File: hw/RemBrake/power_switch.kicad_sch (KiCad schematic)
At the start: 54 parts, among them Q1 SiS415DNT, Q2 BC337, Q3 BC847, Q4 BC337, Q5 BC847, Q6 BC337, Q7 BC847, U1 TPS62140, U2 BD5230G-TR, U3 XC6220B331MR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

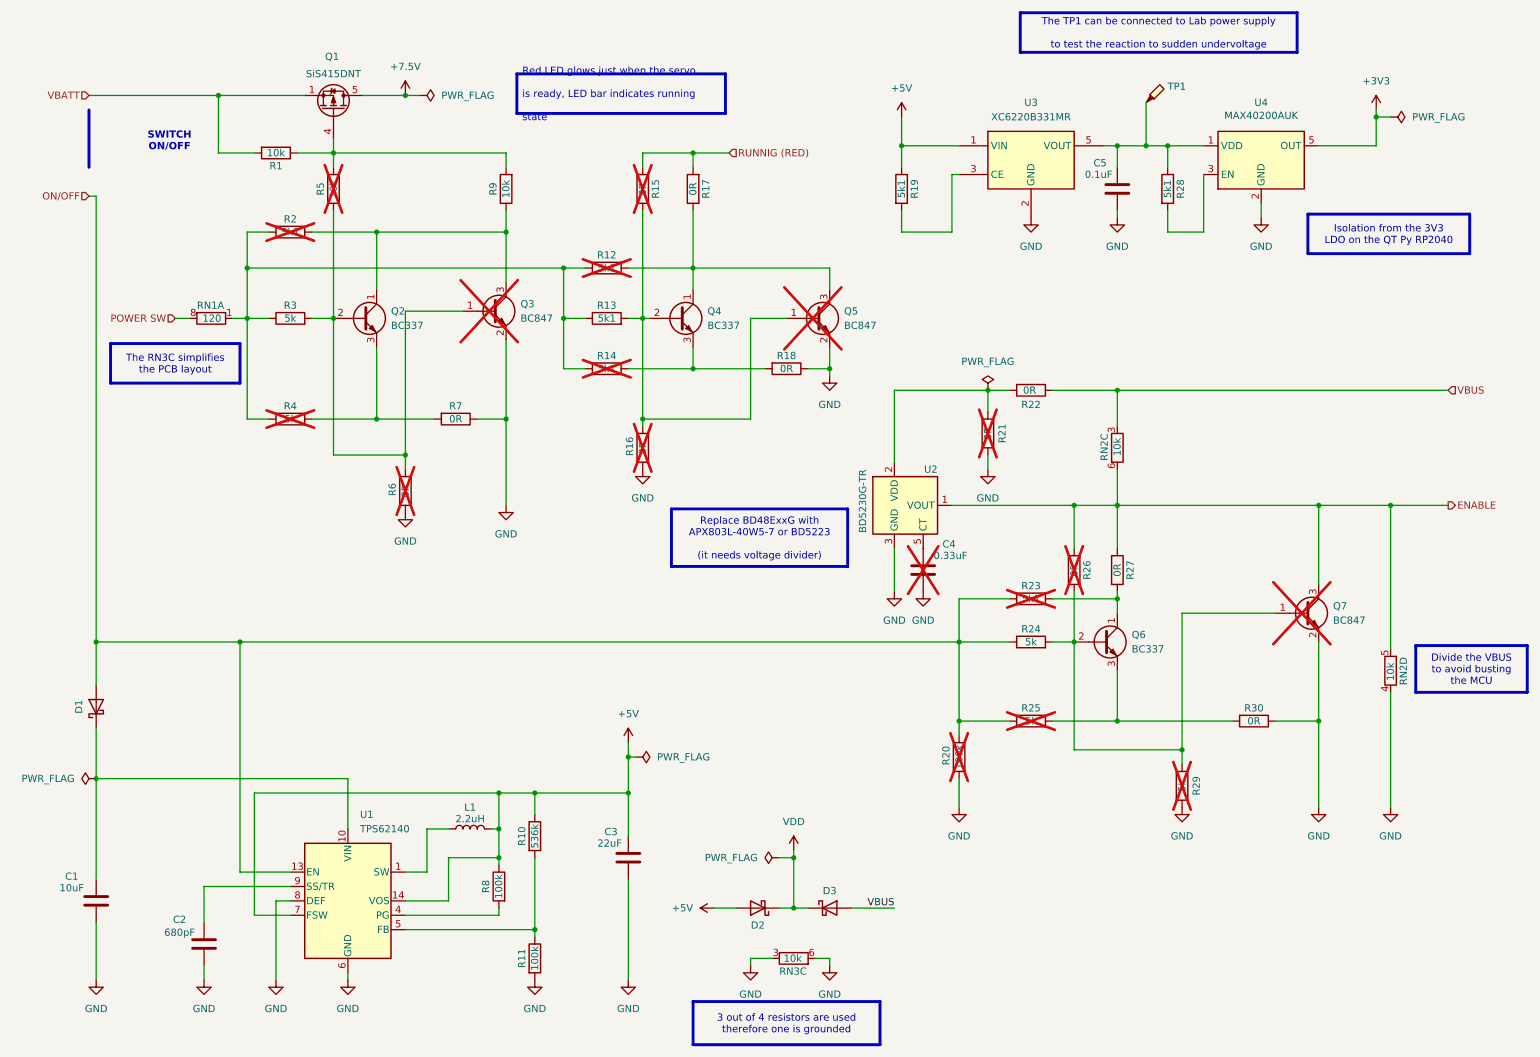
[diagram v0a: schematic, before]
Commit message: updated schematics and pcb - smd transistor was not connected to resistor to limit current through buzzer
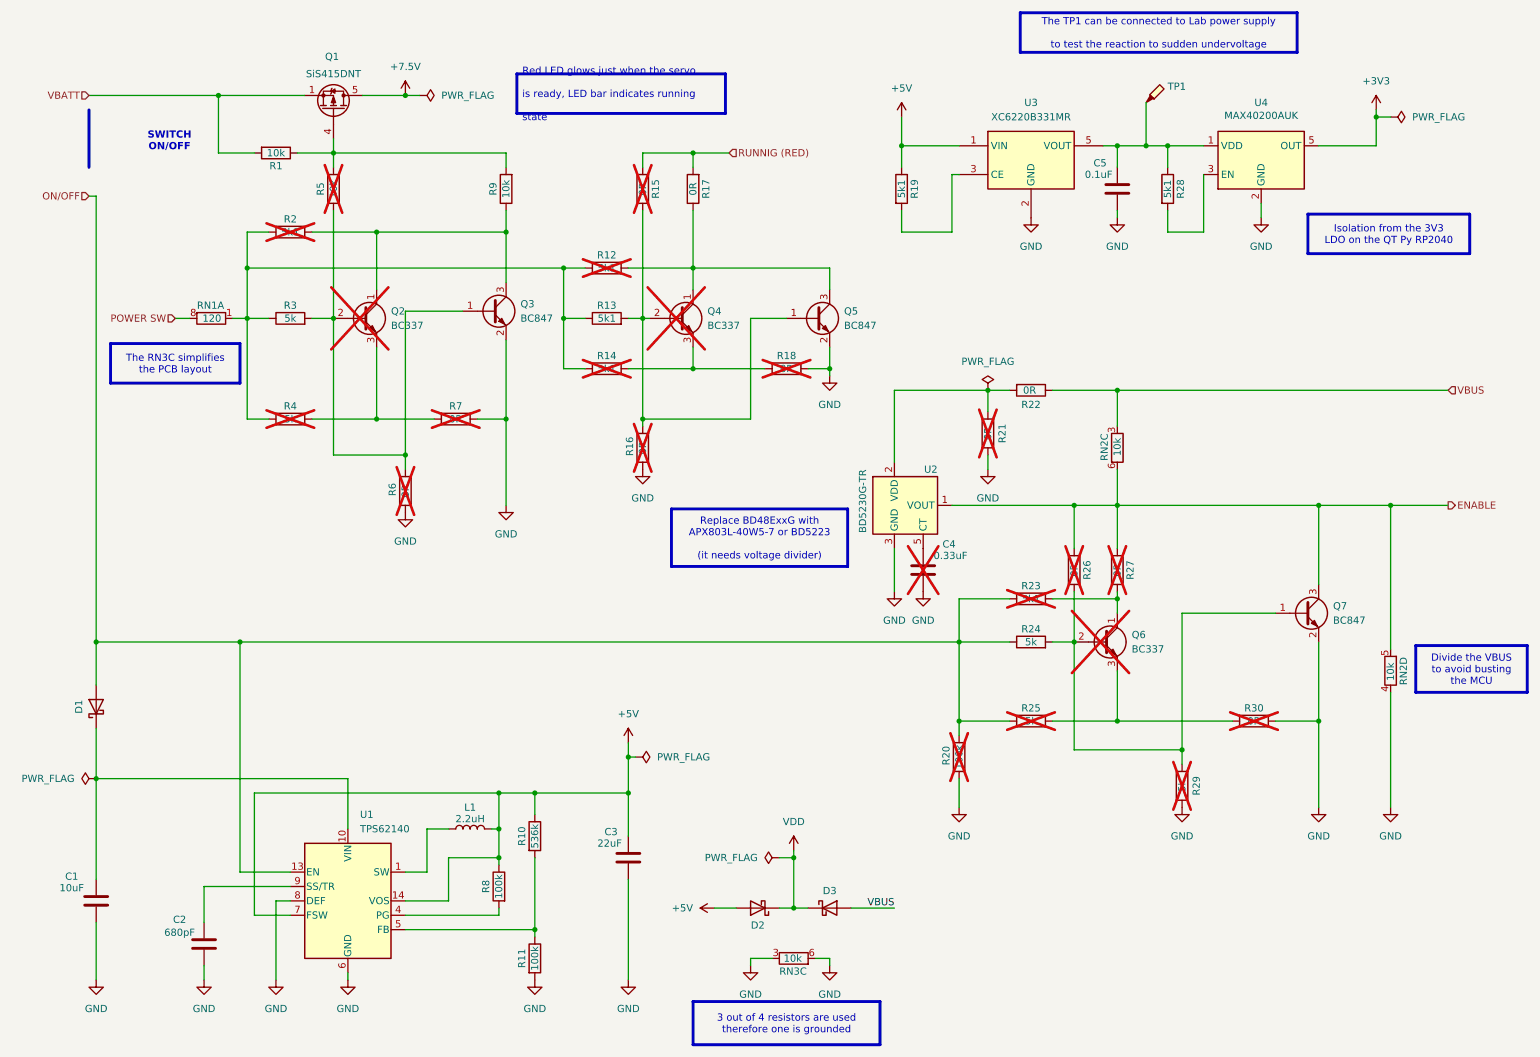
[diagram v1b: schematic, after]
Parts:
- C4: now left out of the parts list
- Q2, Q4, Q6, R18, R27, R30, R7: now not fitted; now left out of the parts list
- Q3, Q5, Q7: now fitted; now in the parts list
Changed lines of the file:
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@@
 		(unit 1)
 		(exclude_from_sim no)
-		(in_bom yes)
+		(in_bom no)
 		(on_board yes)
-		(dnp no)
+		(dnp yes)
 		(fields_autoplaced yes)
 		(property "Reference" "Q2"
@@
 		(unit 1)
 		(exclude_from_sim no)
-		(in_bom no)
+		(in_bom yes)
 		(on_board yes)
-		(dnp yes)
+		(dnp no)
 		(fields_autoplaced yes)
 		(property "Reference" "Q7"
@@
 		(unit 1)
 		(exclude_from_sim no)
-		(in_bom yes)
+		(in_bom no)
 		(on_board yes)
-		(dnp no)
+		(dnp yes)
 		(fields_autoplaced yes)
 		(property "Reference" "Q4"
@@
 		(unit 1)
 		(exclude_from_sim no)
-		(in_bom no)
+		(in_bom yes)
 		(on_board yes)
-		(dnp yes)
+		(dnp no)
 		(fields_autoplaced yes)
 		(property "Reference" "Q3"
@@
 		(unit 1)
 		(exclude_from_sim no)
-		(in_bom yes)
+		(in_bom no)
 		(on_board yes)
-		(dnp no)
+		(dnp yes)
 		(property "Reference" "R18"
 			(at 151.13 73.914 90)
@@
 		(unit 1)
 		(exclude_from_sim no)
-		(in_bom yes)
+		(in_bom no)
 		(on_board yes)
-		(dnp no)
+		(dnp yes)
 		(property "Reference" "R27"
 			(at 211.836 111.76 90)
@@
 		(unit 1)
 		(exclude_from_sim no)
-		(in_bom yes)
+		(in_bom no)
 		(on_board yes)
-		(dnp no)
+		(dnp yes)
 		(property "Reference" "R30"
 			(at 233.68 136.144 90)
@@
 		(unit 1)
 		(exclude_from_sim no)
-		(in_bom yes)
+		(in_bom no)
 		(on_board yes)
-		(dnp no)
+		(dnp yes)
 		(property "Reference" "R7"
 			(at 92.71 82.804 90)
@@
 		(unit 1)
 		(exclude_from_sim no)
-		(in_bom no)
+		(in_bom yes)
 		(on_board yes)
-		(dnp yes)
+		(dnp no)
 		(fields_autoplaced yes)
 		(property "Reference" "Q5"
@@
 		(unit 1)
 		(exclude_from_sim no)
-		(in_bom yes)
+		(in_bom no)
 		(on_board yes)
 		(dnp yes)
@@
 		(unit 1)
 		(exclude_from_sim no)
-		(in_bom yes)
+		(in_bom no)
 		(on_board yes)
-		(dnp no)
+		(dnp yes)
 		(fields_autoplaced yes)
 		(property "Reference" "Q6"

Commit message: removed hopefully last redundant components and updated versions of pcb and schematics
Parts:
- R3: now in the parts list

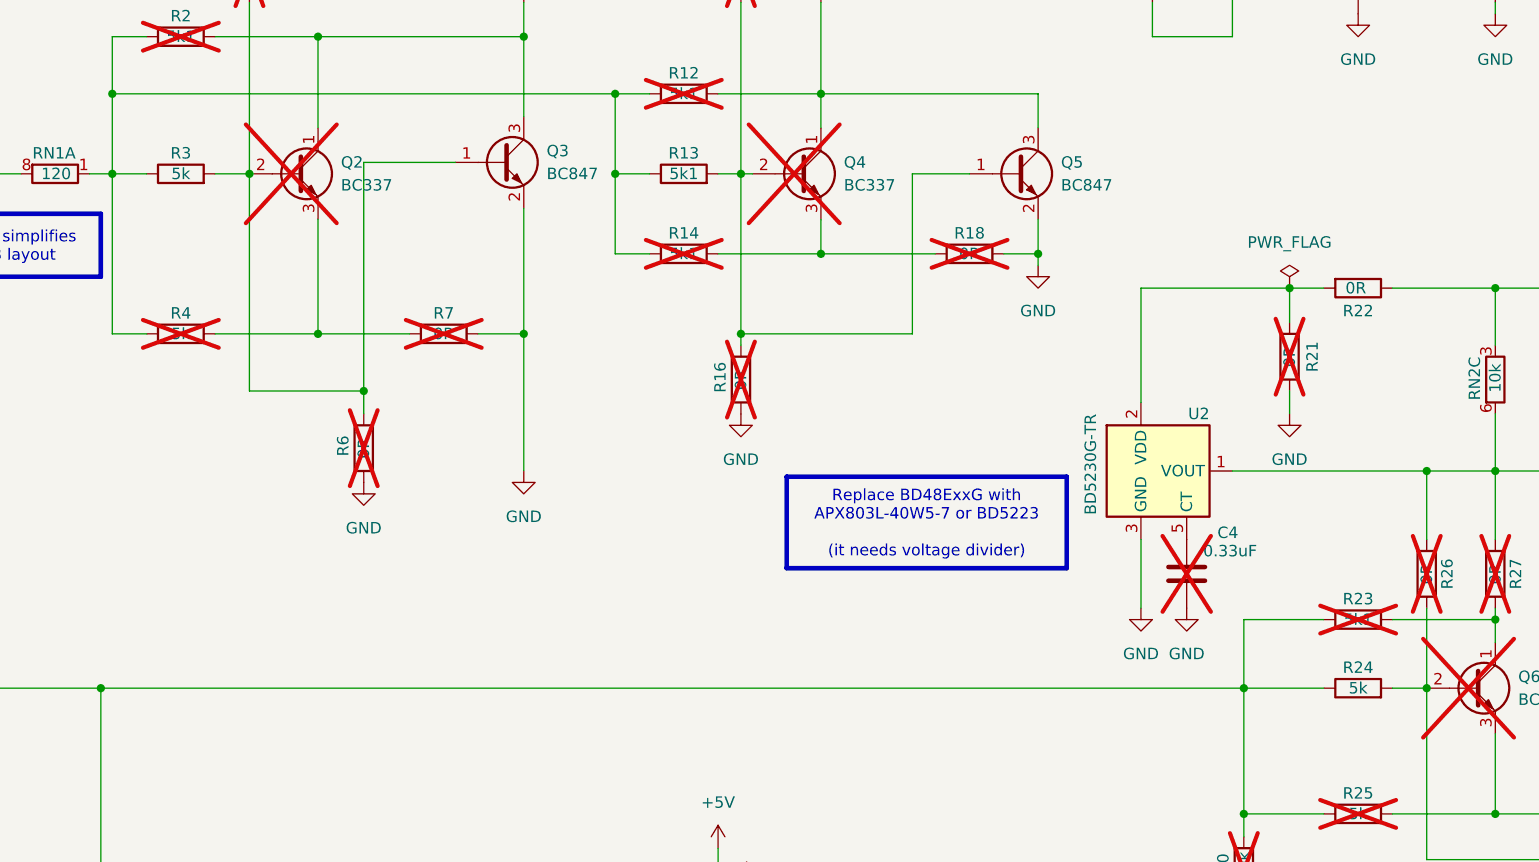
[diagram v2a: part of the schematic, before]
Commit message: 5k resistors replaced by 5k1 resistors
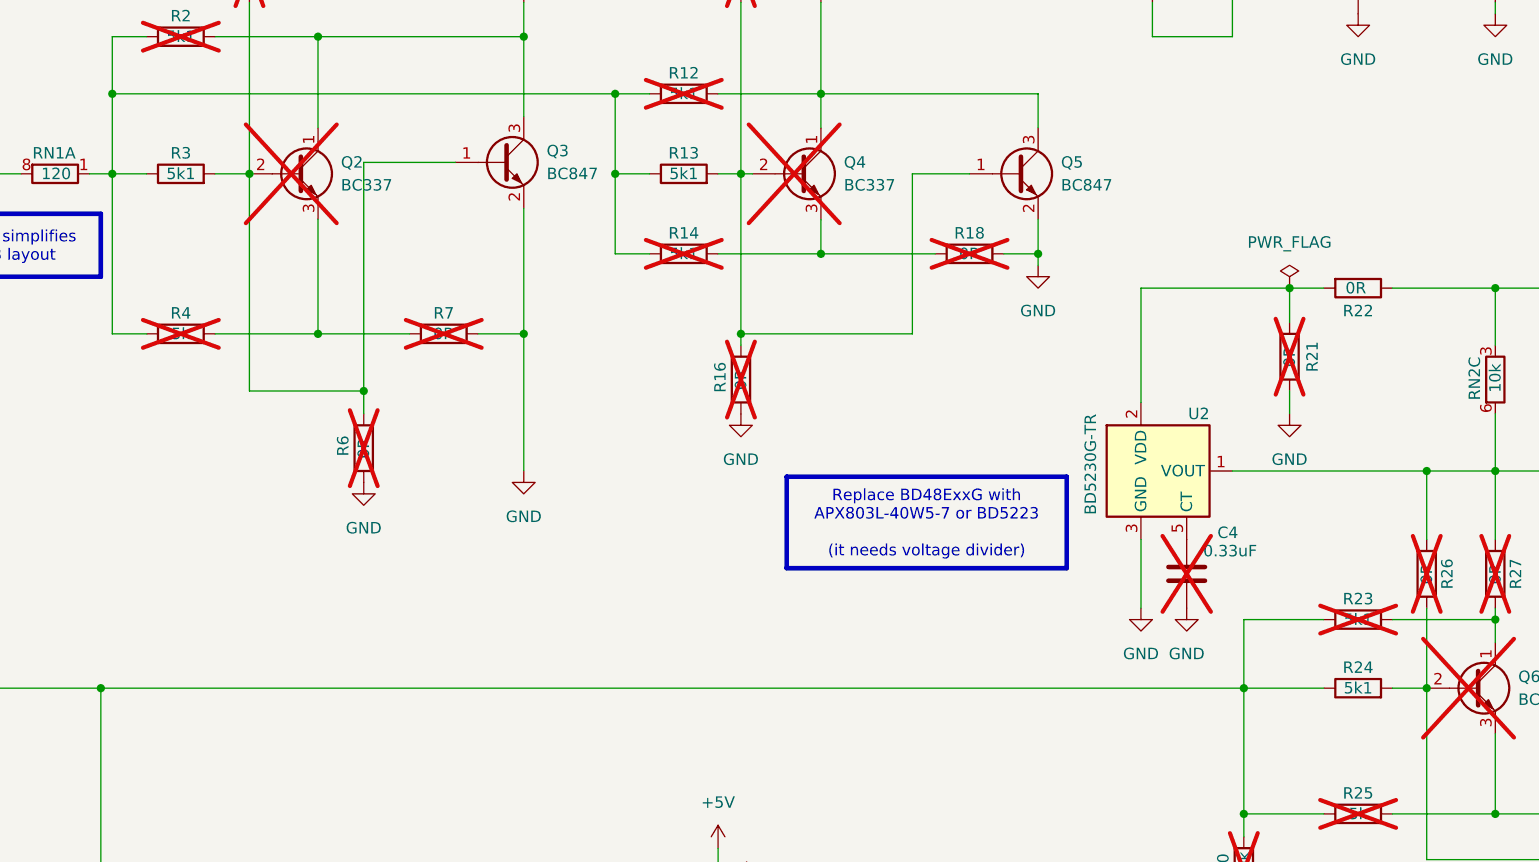
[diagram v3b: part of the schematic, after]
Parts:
- R24, R3: value 5k -> 5k1
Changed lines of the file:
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@@
 			)
 		)
-		(property "Value" "5k"
+		(property "Value" "5k1"
 			(at 194.31 124.46 90)
 			(effects
@@
 			)
 		)
-		(property "Value" "5k"
+		(property "Value" "5k1"
 			(at 63.5 67.31 90)
 			(effects

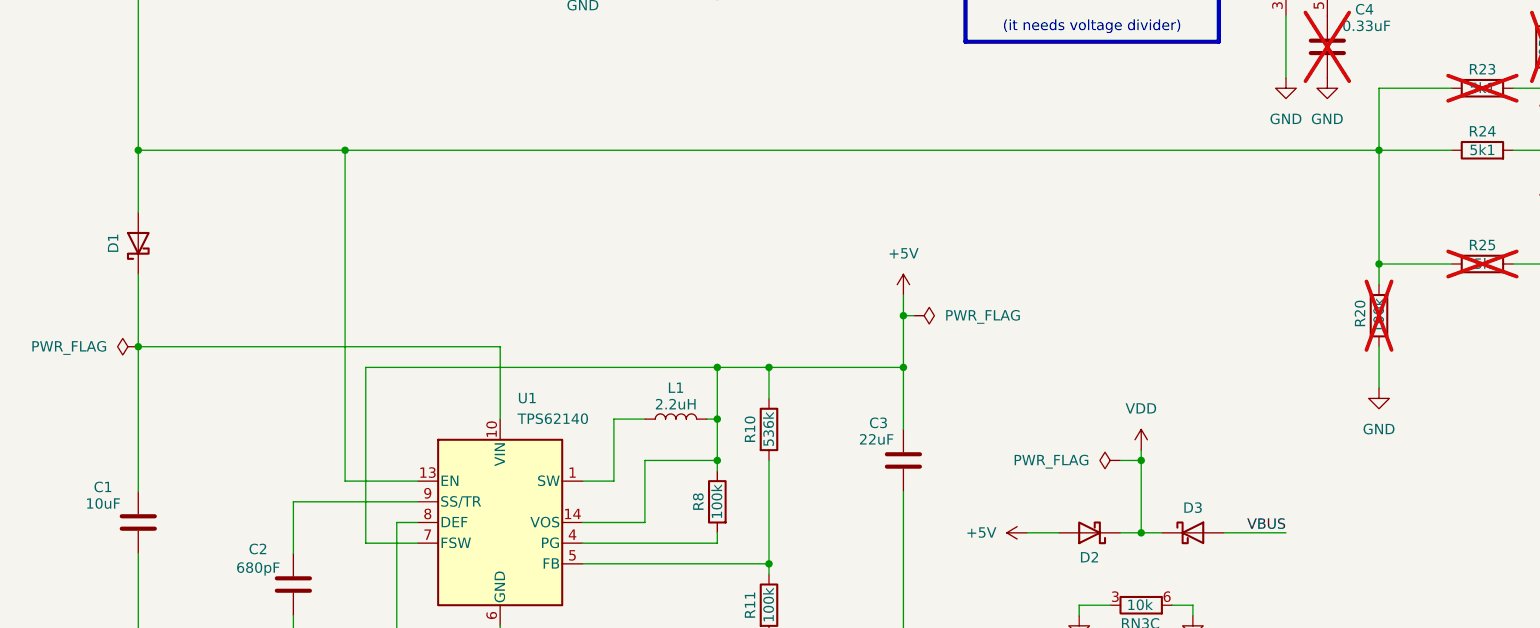
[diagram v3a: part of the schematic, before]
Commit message: updated pcb and added Notes about possible faults
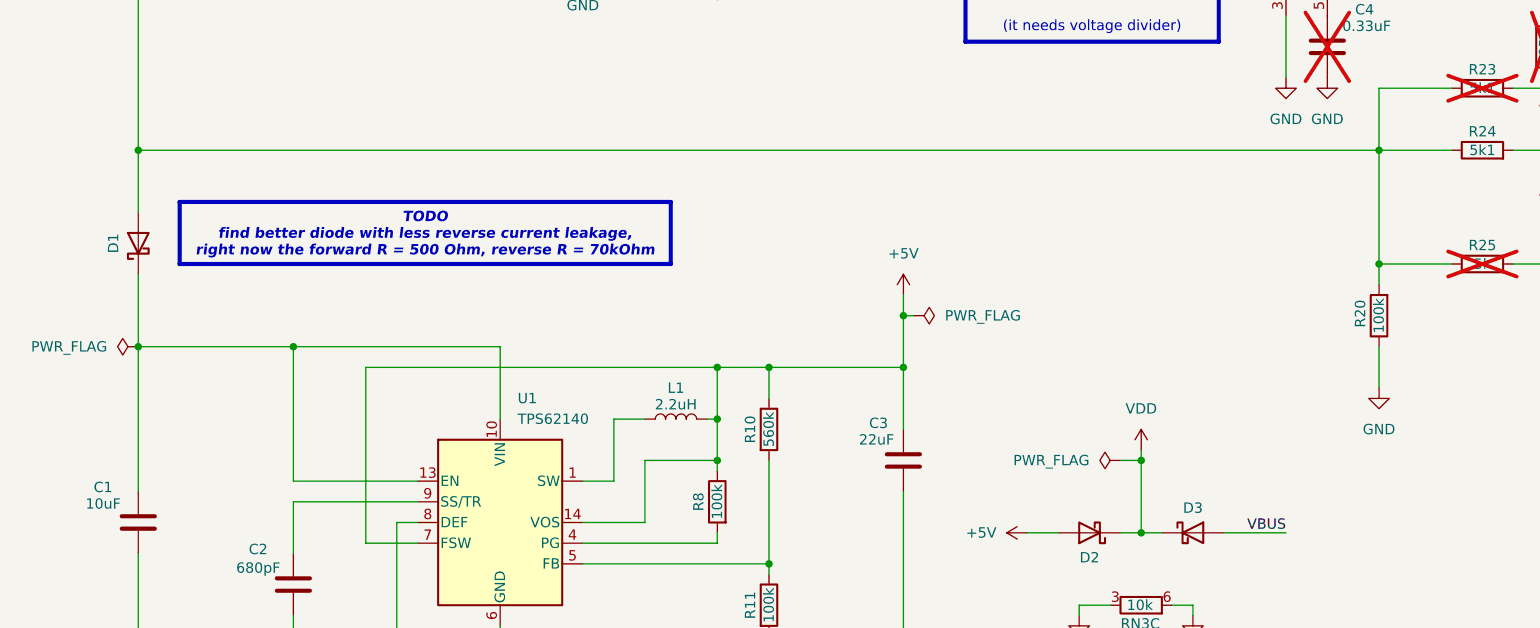
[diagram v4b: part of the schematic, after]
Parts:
- R10: value 536k -> 560k
- R20: now fitted; now in the parts list
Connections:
- net ON/OFF: no longer U1.13 (EN)
- net at C1.1, D1.1 (K), U1.10 (VIN)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: now also U1.13 (EN)
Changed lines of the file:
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@@
 		)
 	)
+	(text_box "TODO\nfind better diode with less reverse current leakage,\nright now the forward R = 500 Ohm, reverse R = 70kOhm"
+		(exclude_from_sim no)
+		(at 34.29 130.81 0)
+		(size 60.325 7.62)
+		(margins 0.9525 0.9525 0.9525 0.9525)
+		(stroke
+			(width 0.508)
+			(type solid)
+			(color 128 63 0 1)
+		)
+		(fill
+			(type color)
+			(color 255 255 153 1)
+		)
+		(effects
+			(font
+				(size 1.27 1.27)
+				(thickness 0.254)
+				(bold yes)
+				(italic yes)
+			)
+		)
+	)
 	(text_box "Isolation from the 3V3 \nLDO on the QT Py RP2040"
 		(exclude_from_sim no)
@@
 	)
 	(junction
+		(at 48.26 148.59)
+		(diameter 0)
+		(color 0 0 0 0)
+	)
+	(junction
 		(at 100.33 162.56)
 		(diameter 0)
@@
 	)
 	(junction
-		(at 54.61 124.46)
-		(diameter 0)
-		(color 0 0 0 0)
-	)
-	(junction
 		(at 125.73 85.09)
 		(diameter 0)
@@
 	(wire
 		(pts
+			(xy 48.26 165.1) (xy 63.5 165.1)
+		)
+		(stroke
+			(width 0)
+			(type default)
+		)
+	)
+	(wire
+		(pts
 			(xy 214.63 29.21) (xy 214.63 36.83)
 		)
@@
 	(wire
 		(pts
+			(xy 48.26 165.1) (xy 48.26 148.59)
+		)
+		(stroke
+			(width 0)
+			(type default)
+		)
+	)
+	(wire
+		(pts
 			(xy 57.15 172.72) (xy 57.15 151.13)
 		)
@@
 	(wire
 		(pts
-			(xy 54.61 165.1) (xy 63.5 165.1)
-		)
-		(stroke
-			(width 0)
-			(type default)
-		)
-	)
-	(wire
-		(pts
 			(xy 78.74 85.09) (xy 88.9 85.09)
 		)
@@
 	(wire
 		(pts
-			(xy 29.21 148.59) (xy 73.66 148.59)
+			(xy 29.21 148.59) (xy 48.26 148.59)
 		)
 		(stroke
@@
 	(wire
 		(pts
+			(xy 48.26 148.59) (xy 73.66 148.59)
+		)
+		(stroke
+			(width 0)
+			(type default)
+		)
+	)
+	(wire
+		(pts
 			(xy 180.34 41.91) (xy 180.34 52.07)
 		)
@@
 	(wire
 		(pts
-			(xy 54.61 124.46) (xy 181.61 124.46)
+			(xy 29.21 124.46) (xy 181.61 124.46)
 		)
 		(stroke
@@
 	(wire
 		(pts
-			(xy 54.61 124.46) (xy 54.61 165.1)
-		)
-		(stroke
-			(width 0)
-			(type default)
-		)
-	)
-	(wire
-		(pts
 			(xy 201.93 115.57) (xy 201.93 124.46)
 		)
@@
 	(wire
 		(pts
-			(xy 29.21 124.46) (xy 54.61 124.46)
-		)
-		(stroke
-			(width 0)
-			(type default)
-		)
-	)
-	(wire
-		(pts
 			(xy 134.62 58.42) (xy 158.75 58.42)
 		)
@@
 			)
 		)
-		(property "Value" "536k"
+		(property "Value" "560k"
 			(at 106.68 158.75 90)
 			(effects
@@
 		(unit 1)
 		(exclude_from_sim no)
-		(in_bom no)
+		(in_bom yes)
 		(on_board yes)
-		(dnp yes)
+		(dnp no)
 		(property "Reference" "R20"
 			(at 179.324 144.526 90)

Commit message: changed diode footprint at the input of the dc/dc, use the same diode as servo clamping diode
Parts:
- D1: footprint Diode_SMD:D_SOD-123 -> Diode_SMD:D_SMA
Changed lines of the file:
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@@
 			)
 		)
-		(property "Footprint" "Diode_SMD:D_SOD-123"
+		(property "Footprint" "Diode_SMD:D_SMA"
 			(at 29.21 135.89 0)
 			(hide yes)
